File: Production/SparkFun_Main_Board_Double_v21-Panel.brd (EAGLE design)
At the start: 138.2 x 254 mm, 402 parts, among them J1 MICROMOD-2222-C, J10 MICRO-SD-PUSH-PUSH-EXT-PIN, J12 Vertical Qwiic Connector, J14 QWIIC_RIGHT_ANGLE, J15 MICROMOD-2222-C, J18 CORTEX_JTAG_DEBUG_MINIMUM_PTH, J2 Vertical Qwiic Connector, J20 MICRO-SD-PUSH-PUSH-EXT-PIN, J21 MICROMOD_FUNCTION_MAIN, J22 MICROMOD_FUNCTION_MAIN, J25 Vertical Qwiic Connector, J26 QWIIC_RIGHT_ANGLE, J27 MICROMOD-2222-C, J30 CORTEX_JTAG_DEBUG_MINIMUM_PTH, J32 MICRO-SD-PUSH-PUSH-EXT-PIN, J33 MICROMOD_FUNCTION_MAIN, J34 MICROMOD_FUNCTION_MAIN, J4 QWIIC_RIGHT_ANGLE, J5 CORTEX_JTAG_DEBUG_MINIMUM_PTH, J6 MICROMOD_FUNCTION_MAIN, J7 MICROMOD_FUNCTION_MAIN, Q1 3.1A/30V/105mΩ, Q2 20V/4.2A/52mΩ/1.4W, Q3 3.1A/30V/105mΩ, Q4 20V/4.2A/52mΩ/1.4W, Q5 3.1A/30V/105mΩ, Q6 20V/4.2A/52mΩ/1.4W, U1 STG3856QTR, U10 AP7347DQ-33W5-7K-3.3V, U11 MCP73831, U12 AP7361C-33, U13 STG3856QTR, U14 ESD Diode, U15 AP7347DQ-33W5-7K-3.3V, U2 MCP73831, U3 ESD Diode, U4 AP7347DQ-33W5-7K-3.3V, U5 AP7361C-33, U6 MCP73831, U7 AP7361C-33, U8 STG3856QTR, U9 ESD Diode

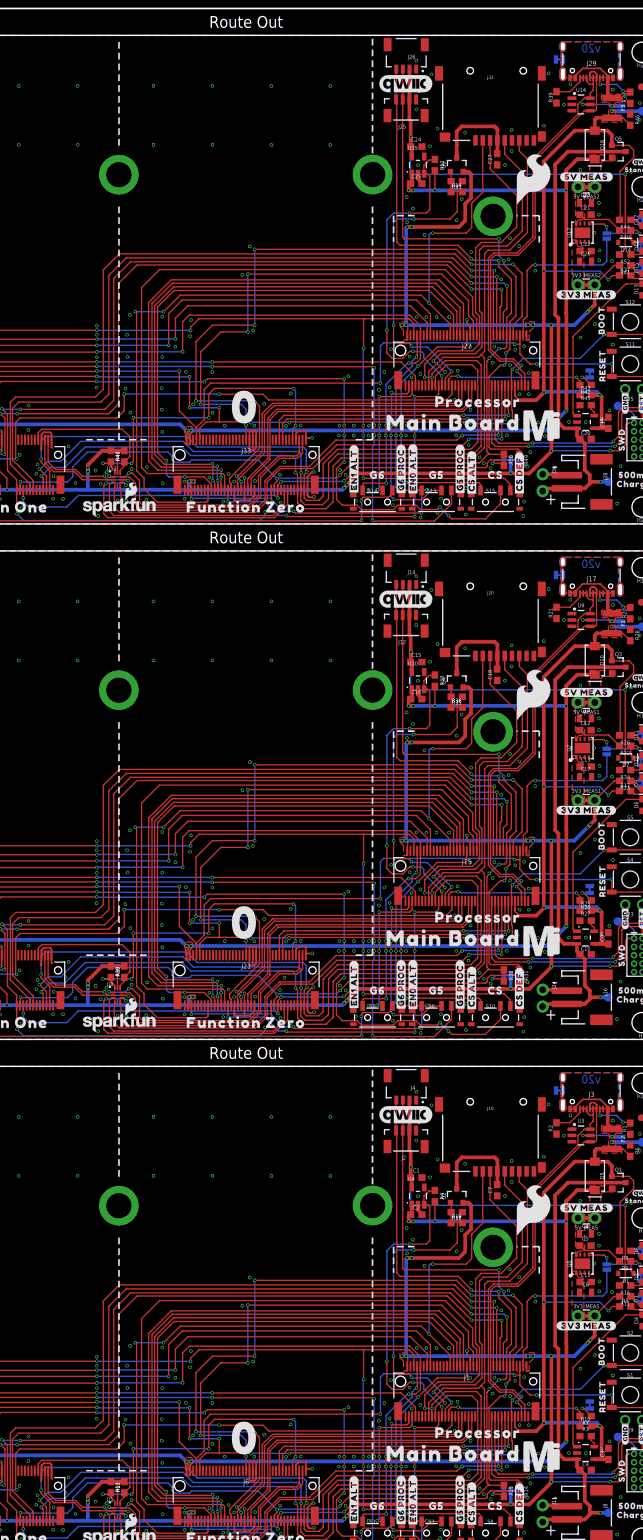
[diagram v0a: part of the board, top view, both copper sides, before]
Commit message: Adds new production panel
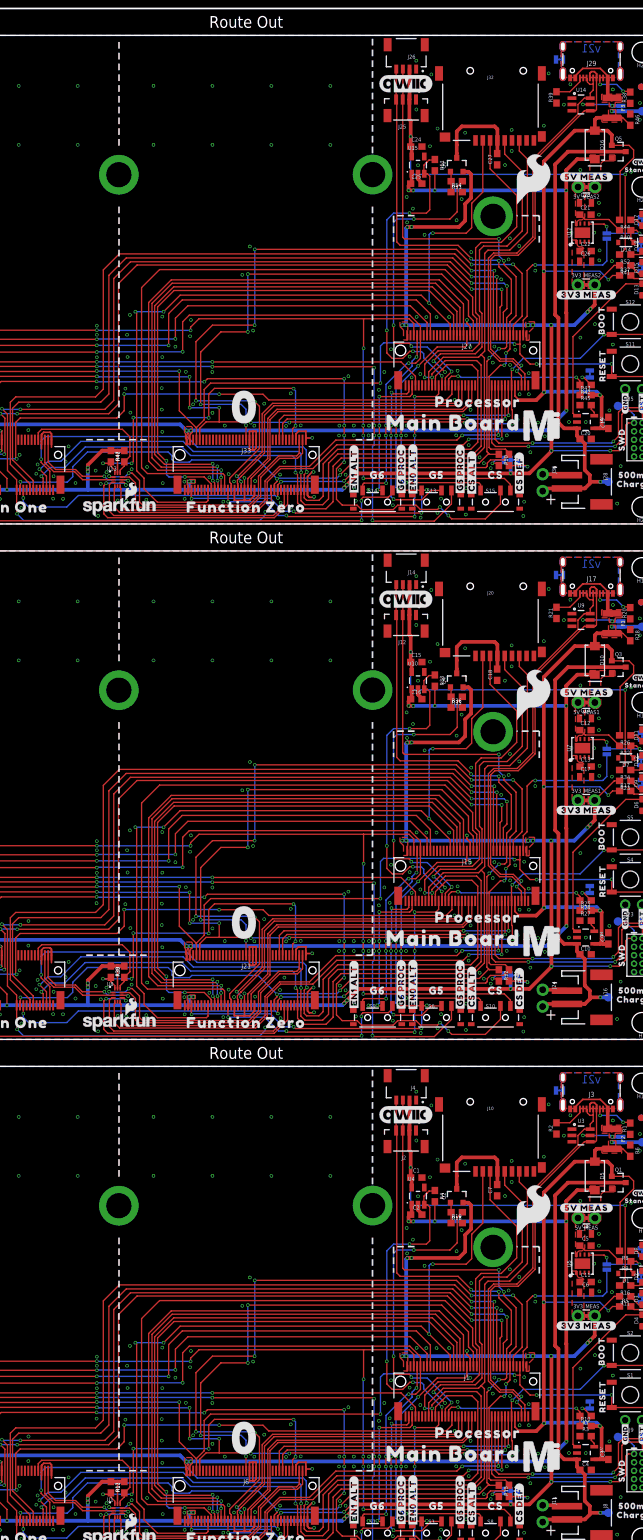
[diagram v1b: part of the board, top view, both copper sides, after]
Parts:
- moved R14 1.52 mm to (101.9, 9.65)
- moved R31 1.52 mm to (101.9, 87.4)
- moved R49 1.52 mm to (101.9, 165.1)
- moved R15 0.76 mm to (100.3, 9.65)
- moved R32 0.76 mm to (100.3, 87.4)
- moved R50 0.76 mm to (100.3, 165.1)
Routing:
- net I2C_SDA2: track 161.7 -> 158.5 mm
- net I2C_SDA1: track 161.7 -> 158.5 mm
- net I2C_SDA: track 161.7 -> 158.5 mm
- net N$11: track 3.74 -> 5.26 mm
- net N$24: track 3.74 -> 5.26 mm
- net N$40: track 3.74 -> 5.26 mm
- net N$41: track 3.78 -> 3.02 mm
- net N$25: track 3.78 -> 3.02 mm
- net N$13: track 3.78 -> 3.02 mm
- net I2C_SCL2: track 157.4 -> 156.7 mm
- net I2C_SCL1: track 157.4 -> 156.7 mm
- net I2C_SCL: track 157.4 -> 156.7 mm
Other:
- board text added: "v21"
- board text removed: "v20"

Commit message: Adds new production files
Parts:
- U$114, U$70: device top:#PTC#503 -> top:#SHLD#501
- U$115, U$71: device top:#SHLD#501 -> top:#I2C#501
- U$116, U$72: device top:#I2C#501 -> top:#3V3_MEAS#6522
- U$117, U$73: device top:#3V3_MEAS#6522 -> top:#5V_MEAS#6522
- U$118, U$74: device top:#5V_MEAS#6522 -> top:500MA6520
- U$119, U$75: device top:500MA6520 -> top:#RST#6521
- U$120, U$76: device top:#RST#6521 -> top:#GND#6520
- U$121, U$77: device top:#GND#6520 -> top:G518
- U$122, U$78: device top:G518 -> top:G6519
- U$123, U$79: device top:G6519 -> top:CS17
- U$124, U$80: device top:CS17 -> top:SWD6522
- U$125, U$81: device top:SWD6522 -> top:#3V3_EN#23
- U$126, U$82: device top:#3V3_EN#23 -> top:#3V3_LED#22
- U$127, U$83: device top:#3V3_LED#22 -> top:#QWIIC_LED#22
- U$128, U$84: device top:#QWIIC_LED#22 -> top:#DIVIDER#23
- U$129, U$85: device top:#DIVIDER#23 -> top:#VIN_LED#24
- U$130, U$86: device top:#VIN_LED#24 -> top:QWC18
- U$131, U$87: device top:QWC18 -> SparkFun-Aesthetics:SFE_LOGO_NAME_FLAME_.1
- U$132, U$88: device SparkFun-Aesthetics:SFE_LOGO_NAME_FLAME_.1 -> top:#PTC#13
- U$3: device top:#PTC#503 -> top:3V332533
- U$45: device top:3V332533 -> top:#PTC#13
- moved U$132 94.3 mm to (115.8, 218.1), flipped to the bottom
- moved U$88 94.3 mm to (115.8, 140.3), flipped to the bottom
- moved U$131 89.6 mm to (43.2, 158.0), turned to 0 degrees
- moved U$87 89.6 mm to (43.2, 80.3), turned to 0 degrees
- moved U$115 59.6 mm to (102.1, 166.9)
- moved U$71 59.6 mm to (102.1, 89.2)
- moved U$45 54.5 mm to (115.8, 62.6), flipped to the bottom, turned to 0 degrees
- moved U$3 54.0 mm to (123.5, 116.6), flipped to the top, turned to 90 degrees
- moved U$118 45.6 mm to (120.9, 162.8)
- moved U$74 45.6 mm to (120.9, 85.1)
- moved U$125 31.2 mm to (112.6, 198.8), flipped to the bottom, turned to 0 degrees
- moved U$81 31.2 mm to (112.6, 121.0), flipped to the bottom, turned to 0 degrees
- moved U$121 30.5 mm to (90.9, 162.8), turned to 0 degrees
- moved U$77 30.5 mm to (90.9, 85.1), turned to 0 degrees
- moved U$116 25.8 mm to (113.5, 190.0), flipped to the top
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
